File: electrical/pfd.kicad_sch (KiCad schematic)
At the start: 9 parts

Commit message: Imrpvoed title of PFD
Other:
- title: PDF -> PFD & ADAHRS
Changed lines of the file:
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@@
   (paper "USLetter" portrait)
   (title_block
-    (title "PDF")
+    (title "PFD & ADAHRS")
     (date "2024-02-03")
     (rev "0.5")

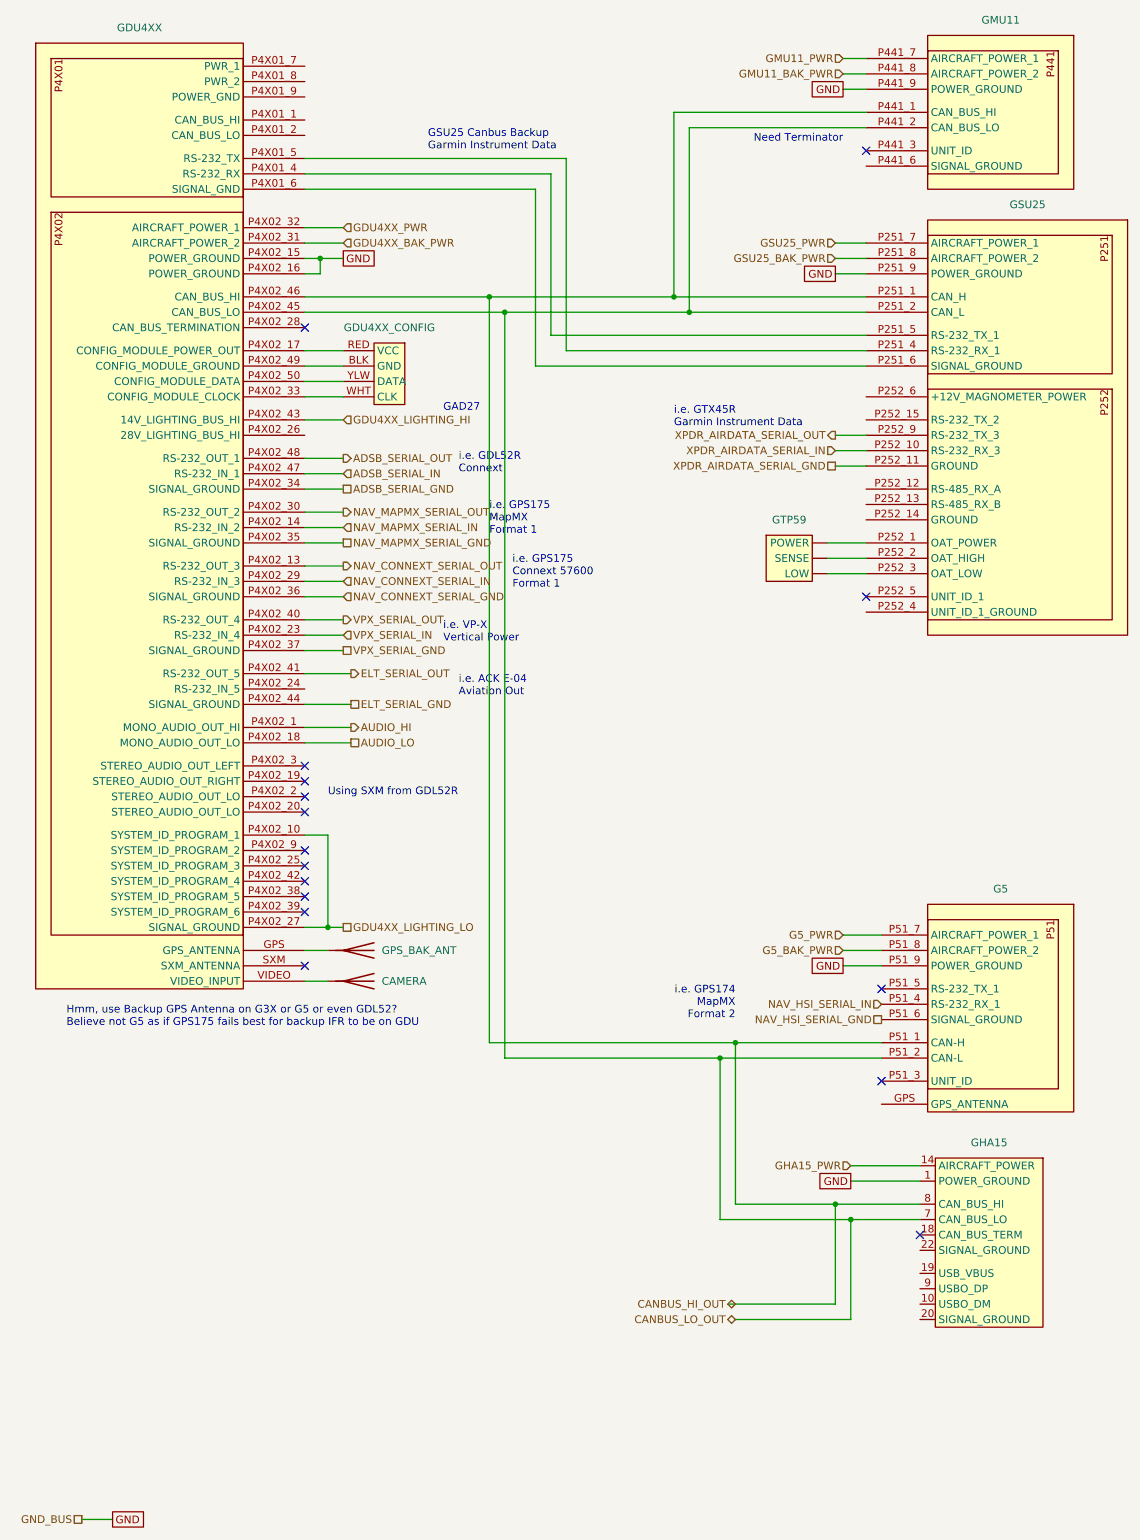
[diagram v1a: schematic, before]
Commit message: Added Transponder and Navigator
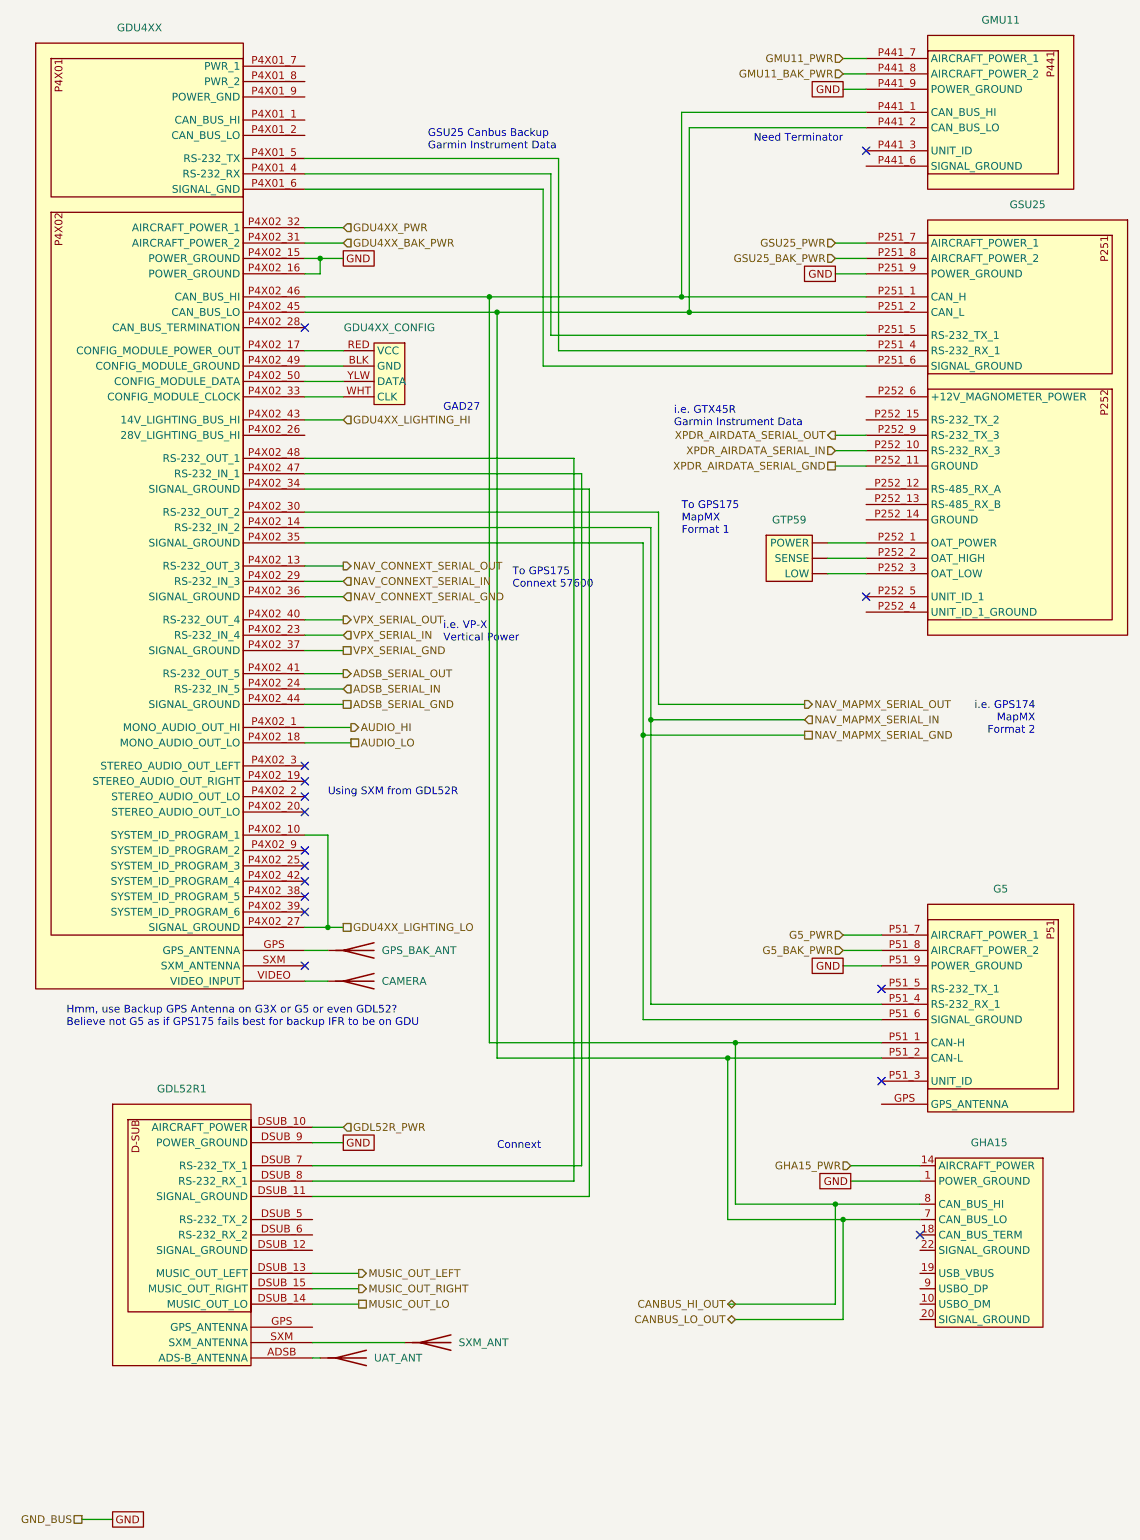
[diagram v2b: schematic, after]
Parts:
- added GDL52R1: ~, symbol flyerx:Garmin_GDL52R
- added SXM_ANT, UAT_ANT: Antenna, symbol Device:Antenna
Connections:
- net ELT_SERIAL_GND is gone; now on net ADSB_SERIAL_GND: GDU4XX.P4X02_44 (SIGNAL_GROUND)
- net ELT_SERIAL_OUT is gone; now on net ADSB_SERIAL_OUT: GDU4XX.P4X02_41 (RS-232_OUT_5)
- net NAV_HSI_SERIAL_GND is gone; now on net NAV_MAPMX_SERIAL_GND: G5.P51_6 (SIGNAL_GROUND)
- net NAV_HSI_SERIAL_IN is gone; now on net NAV_MAPMX_SERIAL_IN: G5.P51_4 (RS-232_RX_1)
- net ADSB_SERIAL_GND: no longer GDU4XX.P4X02_34 (SIGNAL_GROUND)
- net ADSB_SERIAL_IN: now also GDU4XX.P4X02_24 (RS-232_IN_5); no longer GDU4XX.P4X02_47 (RS-232_IN_1)
- net ADSB_SERIAL_OUT: no longer GDU4XX.P4X02_48 (RS-232_OUT_1)
- net GND: now also GDL52R1.DSUB_9 (POWER_GROUND)
- new net: GDL52R1.ADSB (ADS-B_ANTENNA), UAT_ANT.1 (A)
- new net: GDL52R1.DSUB_11 (SIGNAL_GROUND), GDU4XX.P4X02_34 (SIGNAL_GROUND)
- new net: GDL52R1.DSUB_7 (RS-232_TX_1), GDU4XX.P4X02_47 (RS-232_IN_1)
- new net: GDL52R1.DSUB_8 (RS-232_RX_1), GDU4XX.P4X02_48 (RS-232_OUT_1)
- new net: GDL52R1.SXM (SXM_ANTENNA), SXM_ANT.1 (A)
- new net GDL52R_PWR: GDL52R1.DSUB_10 (AIRCRAFT_POWER)
- new net MUSIC_OUT_LEFT: GDL52R1.DSUB_13 (MUSIC_OUT_LEFT)
- new net MUSIC_OUT_LO: GDL52R1.DSUB_14 (MUSIC_OUT_LO)
- new net MUSIC_OUT_RIGHT: GDL52R1.DSUB_15 (MUSIC_OUT_RIGHT)
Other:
- note added: "Connext"
- note added: "To GPS175 Connext 57600"
- note added: "To GPS175 MapMX Format 1"
- note removed: "i.e. ACK E-04 Aviation Out"
- note removed: "i.e. GDL52R Connext"
- note removed: "i.e. GPS175 Connext 57600 Format 1"
- note removed: "i.e. GPS175 MapMX Format 1"

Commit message: Simplified lighting ground
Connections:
- net GDU4XX_LIGHTING_LO: no longer names the net of GDU4XX.P4X02_10 (SYSTEM_ID_PROGRAM_1), GDU4XX.P4X02_27 (SIGNAL_GROUND)
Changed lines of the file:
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@@
   (junction (at 93.98 62.23) (diameter 0) (color 0 0 0 0)
-  )
-  (junction (at 66.04 163.83) (diameter 0) (color 0 0 0 0)
   )
   (junction (at 133.35 182.88) (diameter 0) (color 0 0 0 0)
@@
     (stroke (width 0) (type default))
   )
-  (wire (pts (xy 66.04 163.83) (xy 68.58 163.83))
-    (stroke (width 0) (type default))
-  )
   (wire (pts (xy 125.73 31.75) (xy 125.73 62.23))
     (stroke (width 0) (type default))
@@
     (effects (font (size 1.27 1.27)) (justify right))
   )
-  (hierarchical_label "GDU4XX_LIGHTING_LO" (shape passive) (at 68.58 163.83 0) (fields_autoplaced)
-    (effects (font (size 1.27 1.27)) (justify left))
-  )
   (hierarchical_label "NAV_MAPMX_SERIAL_IN" (shape input) (at 144.78 129.54 0) (fields_autoplaced)

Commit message: Updated with overview
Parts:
- renumbered GDL52R1 to GDL52R, GDU4XX to GDU45X
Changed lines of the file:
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@@
   (symbol (lib_id "flyerx:Garmin_GDL52R") (at 30.48 193.04 0) (unit 1)
     (in_bom yes) (on_board yes) (dnp no) (fields_autoplaced)
-    (property "Reference" "GDL52R1" (at 41.91 190.5 0)
+    (property "Reference" "GDL52R" (at 41.91 190.5 0)
       (effects (font (size 1.27 1.27)))
     )
@@
       (project "electrical"
         (path "/e8ec215a-dbe2-4eba-a577-e50a0a128049/633b5331-dc3f-449e-8212-24f89753723c"
-          (reference "GDL52R1") (unit 1)
+          (reference "GDL52R") (unit 1)
         )
       )
@@
   (symbol (lib_id "flyerx:Garmin_GDU4XX") (at 17.78 17.78 0) (unit 1)
     (in_bom yes) (on_board yes) (dnp no) (fields_autoplaced)
-    (property "Reference" "GDU4XX" (at 34.925 15.24 0)
+    (property "Reference" "GDU45X" (at 34.925 15.24 0)
       (effects (font (size 1.27 1.27)))
     )
@@
       (project "electrical"
         (path "/e8ec215a-dbe2-4eba-a577-e50a0a128049/633b5331-dc3f-449e-8212-24f89753723c"
-          (reference "GDU4XX") (unit 1)
-        )
-      )
+          (reference "GDU45X") (unit 1)
+        )
+      )

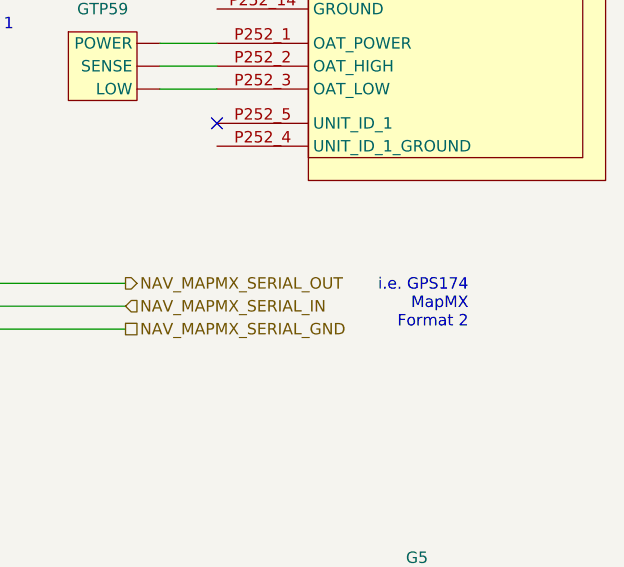
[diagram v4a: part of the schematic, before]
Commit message: Updated system overview and added Power 2 to GTX 45R.
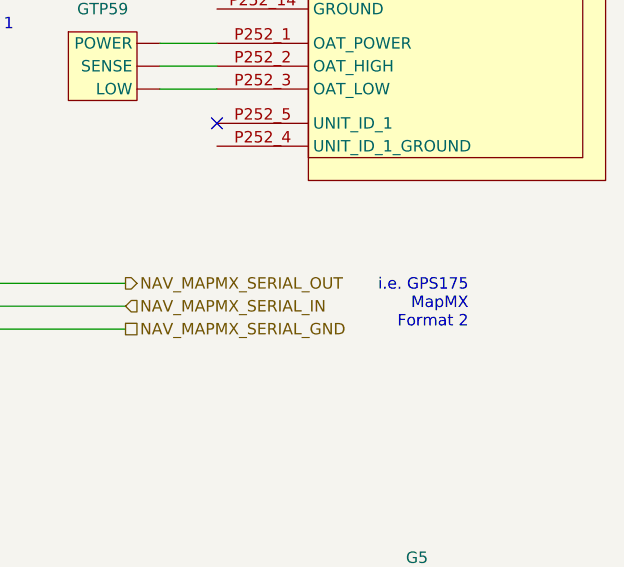
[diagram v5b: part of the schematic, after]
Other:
- note added: "i.e. GPS175 MapMX Format 2"
- note removed: "i.e. GPS174 MapMX Format 2"
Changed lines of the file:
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@@
     (effects (font (size 1.27 1.27)) (justify left bottom))
   )
-  (text "i.e. GPS174\nMapMX\nFormat 2" (at 182.88 132.08 0)
+  (text "i.e. GPS175\nMapMX\nFormat 2" (at 182.88 132.08 0)
     (effects (font (size 1.27 1.27)) (justify right bottom))
   )

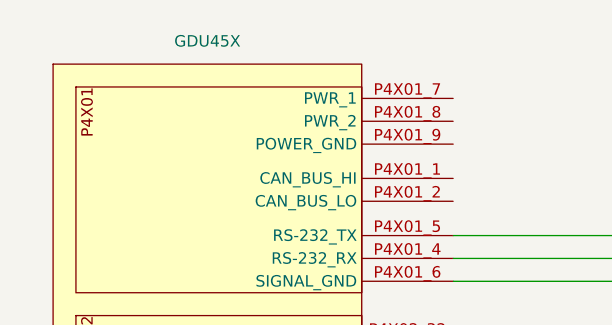
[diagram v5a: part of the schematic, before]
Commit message: Added System overview update with iPad.
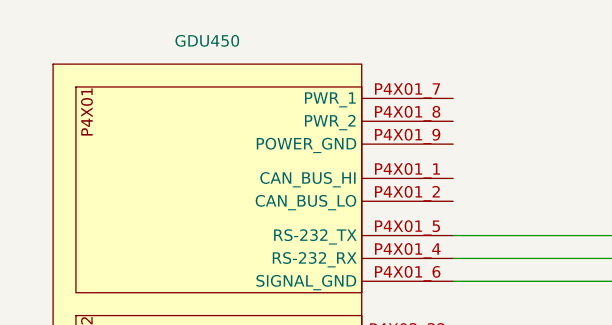
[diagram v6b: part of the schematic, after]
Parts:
- renumbered GDU45X to GDU450
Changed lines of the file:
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@@
   (symbol (lib_id "flyerx:Garmin_GDU4XX") (at 17.78 17.78 0) (unit 1)
     (in_bom yes) (on_board yes) (dnp no) (fields_autoplaced)
-    (property "Reference" "GDU45X" (at 34.925 15.24 0)
+    (property "Reference" "GDU450" (at 34.925 15.24 0)
       (effects (font (size 1.27 1.27)))
     )
@@
       (project "electrical"
         (path "/e8ec215a-dbe2-4eba-a577-e50a0a128049/633b5331-dc3f-449e-8212-24f89753723c"
-          (reference "GDU45X") (unit 1)
+          (reference "GDU450") (unit 1)
         )
       )
